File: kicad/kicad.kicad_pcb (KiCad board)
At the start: 2 copper layers, 50.8 x 22.9 mm, 6 parts

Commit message: updated schematic and pcb
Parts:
- removed @HOLE0, @HOLE1: , 
- removed JP1: , 1X16_ROUND
- removed JP3: , 1X12_ROUND
- removed U$31, U$32: MOUNTINGHOLE2.5, MOUNTINGHOLE_2.5_PLATED
- added A1: Adafruit_Feather_V2, Module:Adafruit_Feather, F.Cu at (188.1, 25.4)
- added D1: 1N4148, PCM_Diode_THT_AKL:D_DO-35_SOD27_P7.62mm_Horizontal, F.Cu at (142.9, 61.9)
- added D10: 1N4148, PCM_Diode_THT_AKL:D_DO-35_SOD27_P7.62mm_Horizontal, F.Cu at (142.9, 119.1)
- added D11: 1N4148, PCM_Diode_THT_AKL:D_DO-35_SOD27_P7.62mm_Horizontal, F.Cu at (161.9, 119.1)
- added D12: 1N4148, PCM_Diode_THT_AKL:D_DO-35_SOD27_P7.62mm_Horizontal, F.Cu at (181.0, 119.1)
- added D2: 1N4148, PCM_Diode_THT_AKL:D_DO-35_SOD27_P7.62mm_Horizontal, F.Cu at (161.9, 61.9)
- added D3: 1N4148, PCM_Diode_THT_AKL:D_DO-35_SOD27_P7.62mm_Horizontal, F.Cu at (181.0, 61.9)
- added D4: 1N4148, PCM_Diode_THT_AKL:D_DO-35_SOD27_P7.62mm_Horizontal, F.Cu at (142.9, 81.0)
- added D5: 1N4148, PCM_Diode_THT_AKL:D_DO-35_SOD27_P7.62mm_Horizontal, F.Cu at (161.9, 81.0)
- added D6: 1N4148, PCM_Diode_THT_AKL:D_DO-35_SOD27_P7.62mm_Horizontal, F.Cu at (181.0, 81.0)
- added D7: 1N4148, PCM_Diode_THT_AKL:D_DO-35_SOD27_P7.62mm_Horizontal, F.Cu at (142.9, 100.0)
- added D8: 1N4148, PCM_Diode_THT_AKL:D_DO-35_SOD27_P7.62mm_Horizontal, F.Cu at (161.9, 100.0)
- added D9: 1N4148, PCM_Diode_THT_AKL:D_DO-35_SOD27_P7.62mm_Horizontal, F.Cu at (181.0, 100.0)
- added S1: Keyswitch, PCM_Switch_Keyboard_Hotswap_Kailh:SW_Hotswap_Kailh_MX_1.00u, F.Cu at (133.3, 57.1)
- added S10: Keyswitch, PCM_Switch_Keyboard_Hotswap_Kailh:SW_Hotswap_Kailh_MX_1.00u, F.Cu at (133.3, 114.3)
- added S11: Keyswitch, PCM_Switch_Keyboard_Hotswap_Kailh:SW_Hotswap_Kailh_MX_1.00u, F.Cu at (152.4, 114.3)
- added S12: Keyswitch, PCM_Switch_Keyboard_Hotswap_Kailh:SW_Hotswap_Kailh_MX_1.00u, F.Cu at (171.4, 114.3)
- added S2: Keyswitch, PCM_Switch_Keyboard_Hotswap_Kailh:SW_Hotswap_Kailh_MX_1.00u, F.Cu at (152.4, 57.1)
- added S3: Keyswitch, PCM_Switch_Keyboard_Hotswap_Kailh:SW_Hotswap_Kailh_MX_1.00u, F.Cu at (171.4, 57.1)
- added S4: Keyswitch, PCM_Switch_Keyboard_Hotswap_Kailh:SW_Hotswap_Kailh_MX_1.00u, F.Cu at (133.3, 76.2)
- added S5: Keyswitch, PCM_Switch_Keyboard_Hotswap_Kailh:SW_Hotswap_Kailh_MX_1.00u, F.Cu at (152.4, 76.2)
- added S6: Keyswitch, PCM_Switch_Keyboard_Hotswap_Kailh:SW_Hotswap_Kailh_MX_1.00u, F.Cu at (171.4, 76.2)
- added S7: Keyswitch, PCM_Switch_Keyboard_Hotswap_Kailh:SW_Hotswap_Kailh_MX_1.00u, F.Cu at (133.3, 95.2)
- added S8: Keyswitch, PCM_Switch_Keyboard_Hotswap_Kailh:SW_Hotswap_Kailh_MX_1.00u, F.Cu at (152.4, 95.2)
- added S9: Keyswitch, PCM_Switch_Keyboard_Hotswap_Kailh:SW_Hotswap_Kailh_MX_1.00u, F.Cu at (171.4, 95.2)
- added SW1: RotaryEncoder_Switch, ScottoKeebs_Scotto:Encoder_EC11_MX, F.Cu at (133.3, 38.1)
- added SW2: SW_Wuerth_450301014042, Button_Switch_THT:SW_Slide-03_Wuerth-WS-SLTV_10x2.5x6.4_P2.54mm, F.Cu at (129.0, 26.5)
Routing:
- net COL2: track 0.00 -> 57.2 mm
- net COL1: track 0.00 -> 57.2 mm
- net COL0: track 0.00 -> 57.2 mm
- net ROW3: track 0.00 -> 38.1 mm
- net ROW2: track 0.00 -> 38.1 mm
- net ROW1: track 0.00 -> 38.1 mm
- net ROW0: track 0.00 -> 38.1 mm
- net Net-(D8-A): track 0.00 -> 4.60 mm
- net Net-(D5-A): track 0.00 -> 4.60 mm
- net Net-(D2-A): track 0.00 -> 4.60 mm
- net Net-(D11-A): track 0.00 -> 4.60 mm
- net Net-(D9-A): track 0.00 -> 4.60 mm
- net Net-(D7-A): track 0.00 -> 4.60 mm
- net Net-(D6-A): track 0.00 -> 4.60 mm
- net Net-(D4-A): track 0.00 -> 4.60 mm
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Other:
- board outline removed
- board text removed: "12"
- board text removed: "13"
- board text removed: "14"
- board text removed: "15"
- board text removed: "27"
- board text removed: "32"
- board text removed: "33"
- board text removed: "37"
- board text removed: "3V"
- board text removed: "A0"
- board text removed: "A1"
- board text removed: "A2"
- board text removed: "A3"
- board text removed: "A4"
- board text removed: "A5"
- board text removed: "ANTENNA"
- board text removed: "BAT"
- board text removed: "BATT_CON"
- board text removed: "EN"
- board text removed: "GND"
- board text removed: "MI"
- board text removed: "MO"
- board text removed: "NC"
- board text removed: "QT I2C"
- board text removed: "RST"
- board text removed: "RX"
- board text removed: "SCK"
- board text removed: "SCL"
- board text removed: "SDA"
- board text removed: "TX"
- board text removed: "USB"
- board text removed: "USB C"

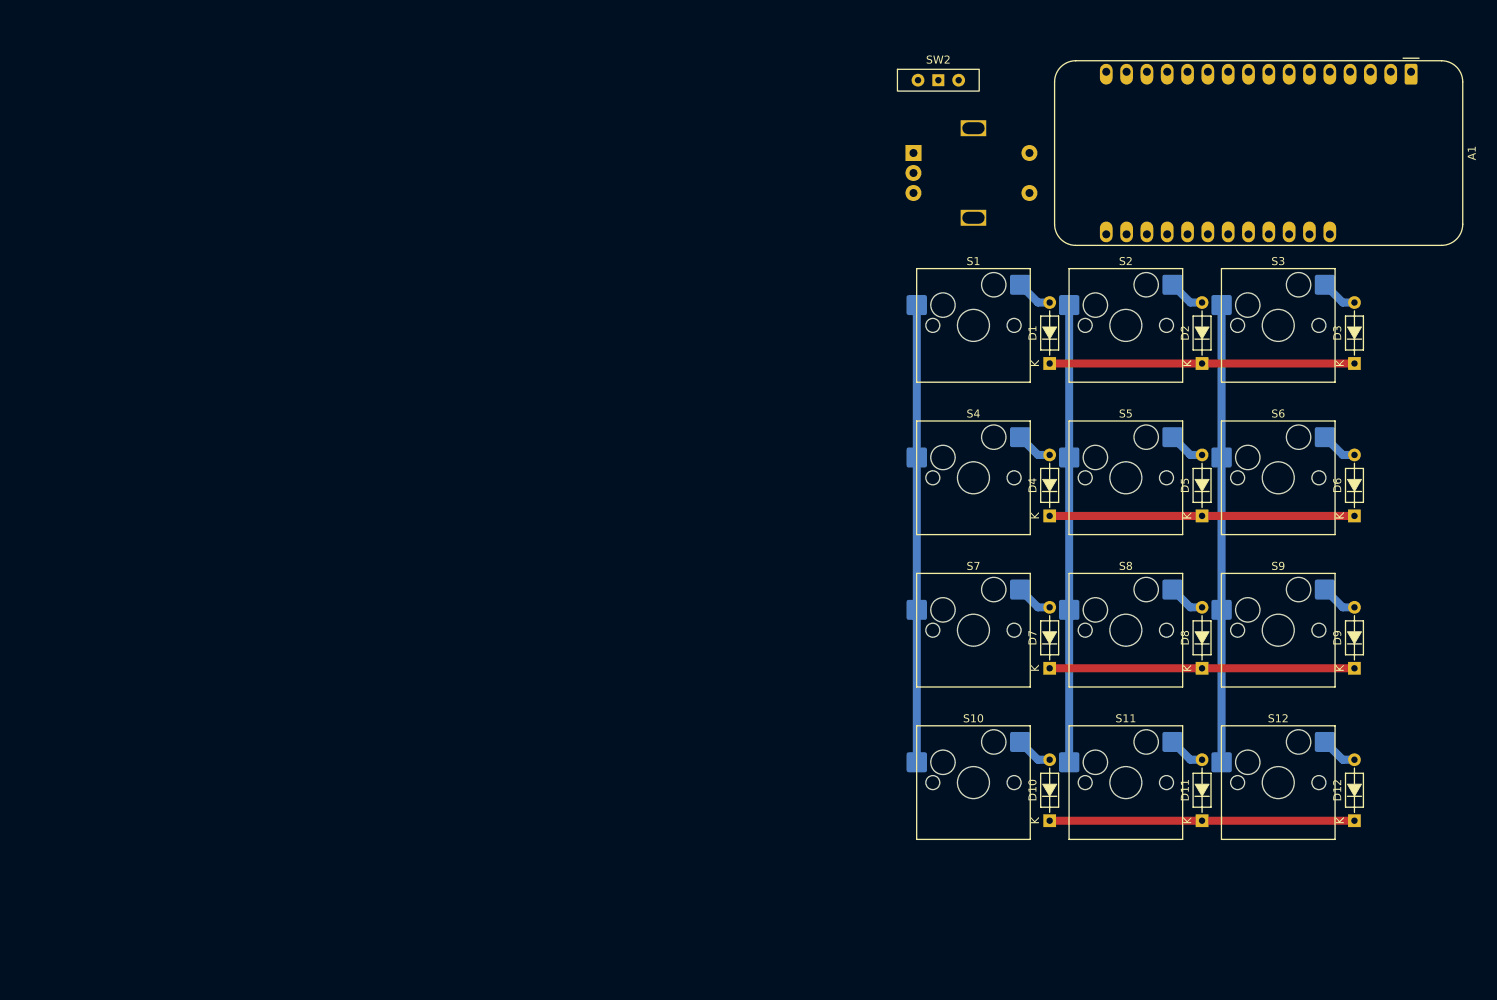
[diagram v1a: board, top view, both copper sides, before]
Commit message: modified layout to be 3 row 4 col instead of 3 col 4 row. added mounting holes
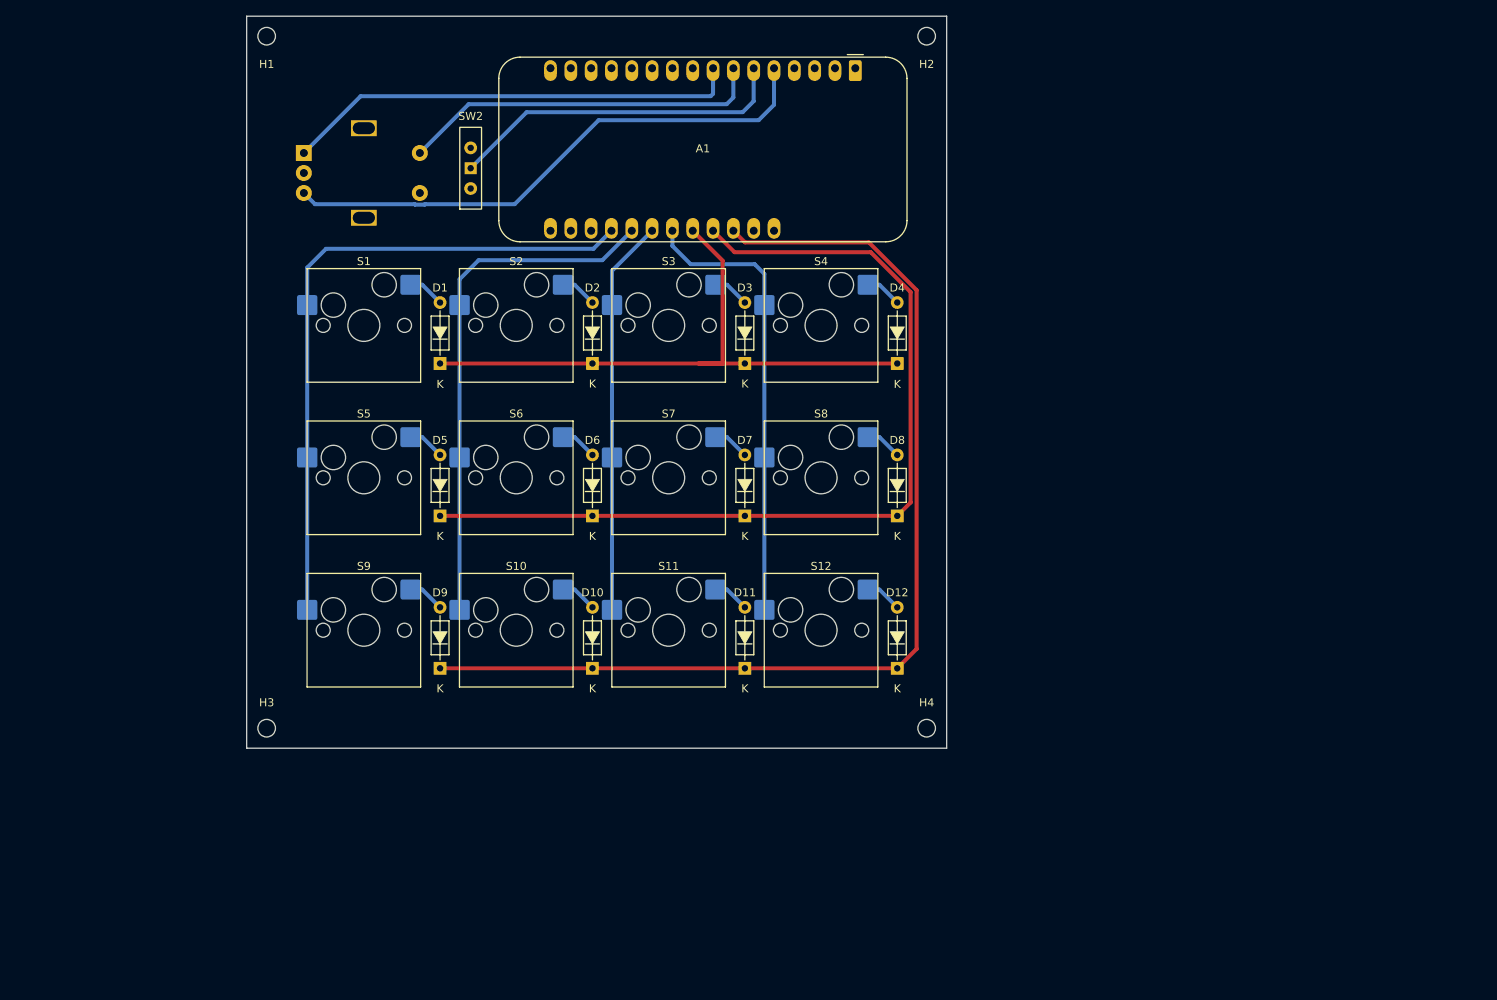
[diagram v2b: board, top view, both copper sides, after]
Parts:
- added H1: MountingHole, MountingHole:MountingHole_2.2mm_M2, F.Cu at (45.0, 21.0)
- added H2: MountingHole, MountingHole:MountingHole_2.2mm_M2, F.Cu at (127.5, 21.0)
- added H3: MountingHole, MountingHole:MountingHole_2.2mm_M2, F.Cu at (45.0, 107.5)
- added H4: MountingHole, MountingHole:MountingHole_2.2mm_M2, F.Cu at (127.5, 107.5)
- moved D9 114.3 mm to (66.7, 100.0)
- moved S9 114.3 mm to (57.1, 95.2)
- moved D5 95.3 mm to (66.7, 81.0)
- moved D6 95.2 mm to (85.7, 81.0)
- moved S5 95.2 mm to (57.1, 76.2)
- moved S6 95.2 mm to (76.2, 76.2)
- moved D2 76.2 mm to (85.7, 61.9)
- moved D1 76.2 mm to (66.7, 61.9)
- moved S2 76.2 mm to (76.2, 57.1)
- moved D3 76.2 mm to (104.8, 61.9)
- moved S1 76.2 mm to (57.1, 57.1)
- moved S3 76.2 mm to (95.2, 57.1)
- moved SW1 76.2 mm to (57.1, 38.1)
- moved A1 69.5 mm to (118.6, 25.0)
- moved D10 60.2 mm to (85.7, 100.0)
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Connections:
- A1 pad 23: ROW0 -> COL3
- A1 pad 24: ROW1 -> ROW0
- A1 pad 25: ROW2 -> ROW1
- A1 pad 26: ROW3 -> ROW2
- A1 pad 5: ENC_CLK -> ENC_DT
- A1 pad 6: ENC_DT -> BT_SELECT
- A1 pad 8: BT_SELECT -> ENC_CLK
- D10 pad 1: ROW3 -> ROW2
- D11 pad 1: ROW3 -> ROW2
- D12 pad 1: ROW3 -> ROW2
- D4 pad 1: ROW1 -> ROW0
- D7 pad 1: ROW2 -> ROW1
- D8 pad 1: ROW2 -> ROW1
- S10 pad 1: COL0 -> COL1
- S11 pad 1: COL1 -> COL2
- S12 pad 1: COL2 -> COL3
- S4 pad 1: COL0 -> COL3
- S5 pad 1: COL1 -> COL0
- S6 pad 1: COL2 -> COL1
- S7 pad 1: COL0 -> COL2
- S8 pad 1: COL1 -> COL3
- S9 pad 1: COL2 -> COL0
- SW1 pad S1: ENC_SW -> GND
- SW1 pad S2: GND -> ENC_SW
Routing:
- net ROW2: track 38.1 -> 131.4 mm
- net ROW1: track 38.1 -> 113.7 mm
- net ENC_DT: track 0.00 -> 69.1 mm
- net ENC_CLK: track 0.00 -> 57.4 mm
- net COL3: track 0.00 -> 56.8 mm
- net ENC_SW: track 0.00 -> 46.9 mm
- net BT_SELECT: track 0.00 -> 43.0 mm
- net ROW0: track 38.1 -> 78.3 mm
- net ROW3: track 38.1 -> 0.00 mm
- net COL0: track 57.2 -> 82.7 mm
- net COL1: track 57.2 -> 65.4 mm
- net COL2: track 57.2 -> 49.5 mm
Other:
- board outline added: 87.5 x 91.5 mm

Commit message: added 3d model for oled 128 x 64. went back to 3 x 4 format
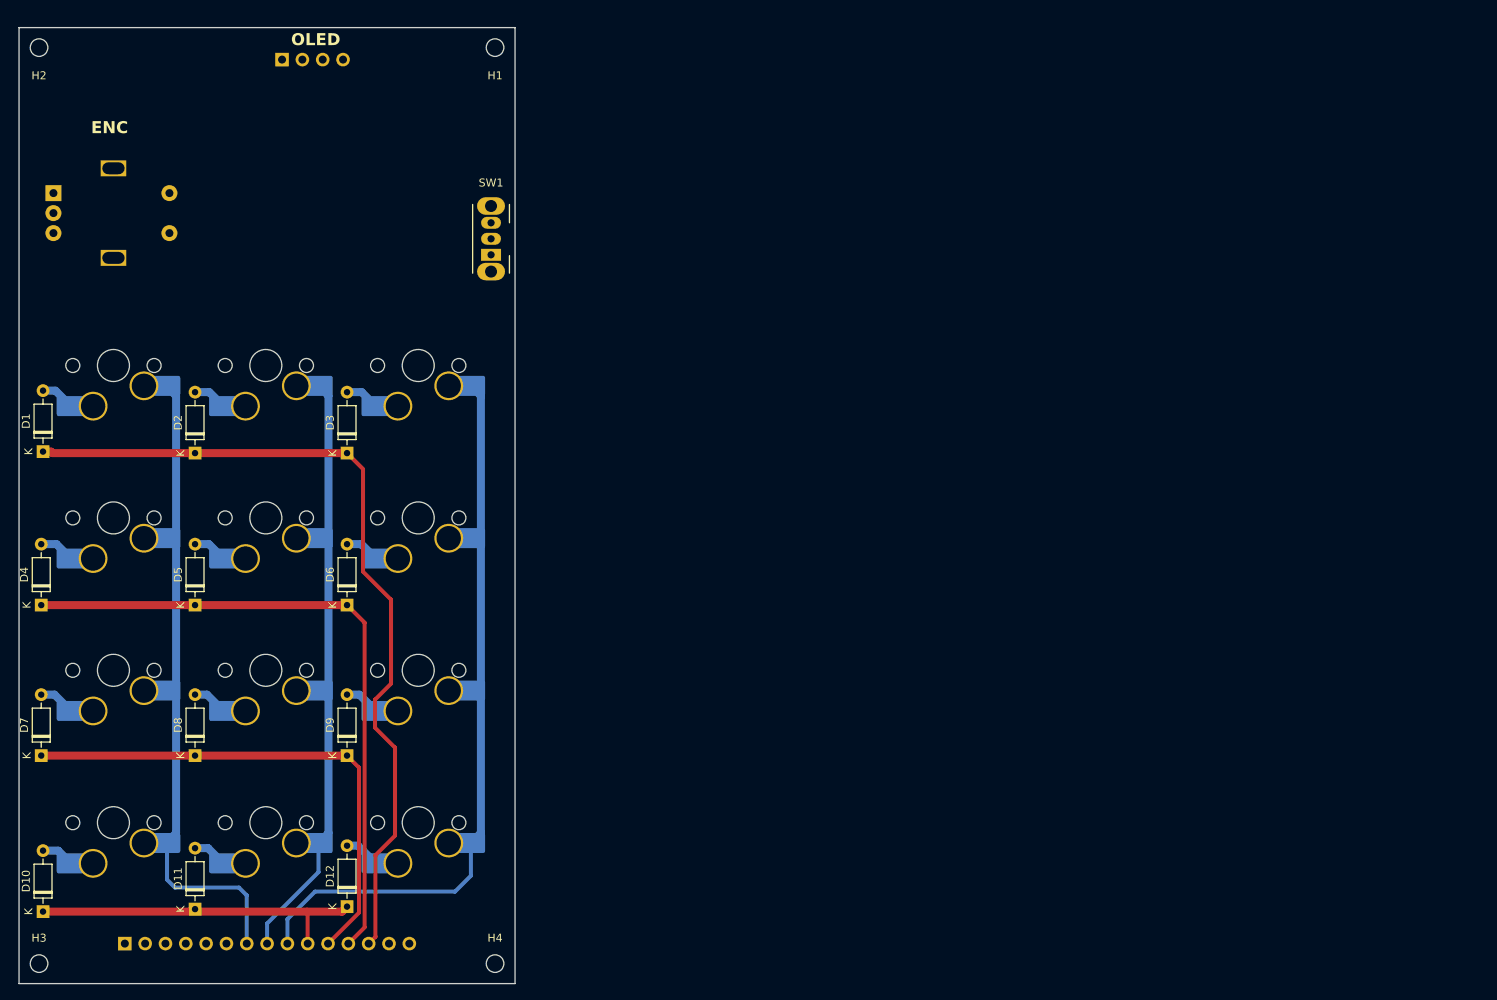
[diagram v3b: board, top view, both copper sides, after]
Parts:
- removed A1: Adafruit_Feather_V2, Module:Adafruit_Feather
- added J1: OLED_128x64, ScottoKeebs_Components:OLED_128x64, F.Cu at (50.7, 23.9)
- added J2: Conn_01x15, Connector_PinHeader_2.54mm:PinHeader_1x15_P2.54mm_Vertical, B.Cu at (27.3, 134.4)
- D1, D10, D11, D12, D2, D3, D4, D5, D6, D7, D8, D9: footprint PCM_Diode_THT_AKL:D_DO-35_SOD27_P7.62mm_Horizontal -> Diode_THT:D_DO-35_SOD27_P7.62mm_Horizontal
- S1, S10, S11, S12, S2, S3, S4, S5, S6, S7, S8, S9: footprint PCM_Switch_Keyboard_Hotswap_Kailh:SW_Hotswap_Kailh_MX_1.00u -> ScottoKeebs_Scotto:MX_Hotswap_1.00u; moved to B.Cu
- SW1: value RotaryEncoder_Switch -> SW_SPDT; footprint ScottoKeebs_Scotto:Encoder_EC11_MX -> Button_Switch_THT:SW_Slide_SPDT_Angled_CK_OS102011MA1Q
- SW2: value SW_Wuerth_450301014042 -> RotaryEncoder_Switch; footprint Button_Switch_THT:SW_Slide-03_Wuerth-WS-SLTV_10x2.5x6.4_P2.54mm -> ScottoKeebs_Scotto:Encoder_EC11_MX
- moved D4 111.2 mm to (16.8, 92.1)
- moved H2 111.0 mm to (16.5, 22.4)
- moved D7 92.9 mm to (16.8, 110.9)
- moved D8 92.8 mm to (36.0, 110.9)
- moved S4 92.1 mm to (26.5, 85.0), turned to 180 degrees
- moved D10 75.1 mm to (17.0, 130.4)
- moved D11 75.0 mm to (36.0, 130.1)
- moved D12 75.0 mm to (55.0, 129.8)
- moved S7 74.2 mm to (26.5, 104.1), turned to 180 degrees
- moved S8 74.2 mm to (45.5, 104.1), turned to 180 degrees
- moved H4 61.5 mm to (73.5, 136.9)
- moved S10 57.0 mm to (26.5, 123.1), turned to 180 degrees
- moved S11 57.0 mm to (45.5, 123.1), turned to 180 degrees
- moved S12 57.0 mm to (64.6, 123.1), turned to 180 degrees
- moved D3 51.0 mm to (55.0, 73.1)
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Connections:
- D10 pad 1: ROW2 -> ROW3
- D11 pad 1: ROW2 -> ROW3
- D12 pad 1: ROW2 -> ROW3
- D4 pad 1: ROW0 -> ROW1
- D7 pad 1: ROW1 -> ROW2
- D8 pad 1: ROW1 -> ROW2
- S10 pad 1: COL1 -> COL0
- S11 pad 1: COL2 -> COL1
- S12 pad 1: COL3 -> COL2
- S4 pad 1: COL3 -> COL0
- S5 pad 1: COL0 -> COL1
- S6 pad 1: COL1 -> COL2
- S7 pad 1: COL2 -> COL0
- S8 pad 1: COL3 -> COL1
- S9 pad 1: COL0 -> COL2
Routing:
- net ENC_DT: track 69.1 -> 0.00 mm
- net ROW2: track 131.4 -> 64.0 mm
- net ENC_CLK: track 57.4 -> 0.00 mm
- net COL3: track 56.8 -> 0.00 mm
- net ENC_SW: track 46.9 -> 0.00 mm
- net BT_SELECT: track 43.0 -> 0.00 mm
- net ROW3: track 0.00 -> 42.3 mm
- net COL2: track 49.5 -> 90.5 mm
- net ROW1: track 113.7 -> 82.3 mm
- net ROW0: track 78.3 -> 104.9 mm
- net COL1: track 65.4 -> 73.4 mm
- net COL0: track 82.7 -> 79.5 mm
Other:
- board size 87.5 x 91.5 mm -> 62 x 119.5 mm
- board text added: "ENC"
- board text added: "OLED"
